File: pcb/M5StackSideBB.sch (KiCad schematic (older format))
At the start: 4 parts, among them J1 Conn_01x15, J2 Conn_01x15, J3 Conn_02x15_Odd_Even, J4 Conn_02x15_Odd_Even

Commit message: Put components and holes as pcb
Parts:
- removed J1, J2: Conn_01x15, Connector_PinSocket_2.54mm:PinSocket_1x15_P2.54mm_Vertical, symbol Connector_Generic:Conn_01x15
- added J1: Conn_01x17, Connector_PinSocket_2.54mm:PinSocket_1x17_P2.54mm_Vertical, symbol Connector_Generic:Conn_01x17
- added J2: Conn_01x09, Connector_PinSocket_2.54mm:PinSocket_1x09_P2.54mm_Vertical, symbol Connector_Generic:Conn_01x09
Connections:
- net labels added: +3.3V
- net labels removed: 3V3

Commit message: Update schema and put silk texts
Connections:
- wire segments 42 -> 43
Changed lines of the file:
@@
 L power:+5V #PWR0114
 U 1 1 5B27E3D3
-P 5450 3350
-F 0 "#PWR0114" H 5450 3200 50  0001 C CNN
-F 1 "+5V" H 5465 3523 50  0000 C CNN
-F 2 "" H 5450 3350 50  0001 C CNN
-F 3 "" H 5450 3350 50  0001 C CNN
-	1    5450 3350
+P 5450 3450
+F 0 "#PWR0114" H 5450 3300 50  0001 C CNN
+F 1 "+5V" H 5465 3623 50  0000 C CNN
+F 2 "" H 5450 3450 50  0001 C CNN
+F 3 "" H 5450 3450 50  0001 C CNN
+	1    5450 3450
 	1    0    0    -1
 $EndComp
@@
 L power:+3.3V #PWR0115
 U 1 1 5B27E3D9
-P 5600 3250
-F 0 "#PWR0115" H 5600 3100 50  0001 C CNN
-F 1 "+3.3V" H 5615 3423 50  0000 C CNN
-F 2 "" H 5600 3250 50  0001 C CNN
-F 3 "" H 5600 3250 50  0001 C CNN
-	1    5600 3250
+P 5600 3350
+F 0 "#PWR0115" H 5600 3200 50  0001 C CNN
+F 1 "+3.3V" H 5615 3523 50  0000 C CNN
+F 2 "" H 5600 3350 50  0001 C CNN
+F 3 "" H 5600 3350 50  0001 C CNN
+	1    5600 3350
 	1    0    0    -1
 $EndComp
@@
 L power:GND #PWR0116
 U 1 1 5B27E3DF
-P 5750 3450
-F 0 "#PWR0116" H 5750 3200 50  0001 C CNN
-F 1 "GND" H 5755 3277 50  0000 C CNN
-F 2 "" H 5750 3450 50  0001 C CNN
-F 3 "" H 5750 3450 50  0001 C CNN
-	1    5750 3450
+P 5850 3650
+F 0 "#PWR0116" H 5850 3400 50  0001 C CNN
+F 1 "GND" H 5855 3477 50  0000 C CNN
+F 2 "" H 5850 3650 50  0001 C CNN
+F 3 "" H 5850 3650 50  0001 C CNN
+	1    5850 3650
 	1    0    0    -1
 $EndComp
 Wire Wire Line
-	6000 3250 5600 3250
+	6000 3350 5600 3350
 Wire Wire Line
-	6000 3350 5450 3350
-Wire Wire Line
-	6000 3450 5750 3450
+	6000 3450 5450 3450
 $Comp
 L Connector_Generic:Conn_01x09 J2
@@
 Wire Wire Line
 	3850 2000 4150 2000
+Wire Wire Line
+	6000 3250 5850 3250
+Wire Wire Line
+	5850 3250 5850 3650
 $EndSCHEMATC

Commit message: Change pinsocket on schema
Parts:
- removed J1: Conn_01x17, Connector_PinSocket_2.54mm:PinSocket_1x17_P2.54mm_Vertical, symbol Connector_Generic:Conn_01x17
- removed J2: Conn_01x09, Connector_PinSocket_2.54mm:PinSocket_1x09_P2.54mm_Vertical, symbol Connector_Generic:Conn_01x09
- added J1, J2: Conn_01x11, Connector_PinSocket_2.54mm:PinSocket_1x11_P2.54mm_Vertical, symbol Connector_Generic:Conn_01x11
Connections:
- wire segments 43 -> 36
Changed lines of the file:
@@
 Wire Wire Line
 	7750 2150 7750 2250
-$Comp
-L power:GND #PWR0102
-U 1 1 5B24A9FC
-P 4550 2250
-F 0 "#PWR0102" H 4550 2000 50  0001 C CNN
-F 1 "GND" H 4555 2077 50  0000 C CNN
-F 2 "" H 4550 2250 50  0001 C CNN
-F 3 "" H 4550 2250 50  0001 C CNN
-	1    4550 2250
-	1    0    0    -1
-$EndComp
-Text GLabel 4150 2500 0    39   Input ~ 0
+Text GLabel 4950 2350 0    39   Input ~ 0
 G2
-Text GLabel 6000 3150 0    39   Input ~ 0
+Text GLabel 6000 2950 0    39   Input ~ 0
 G21
-Text GLabel 4150 2300 0    39   Input ~ 0
+Text GLabel 6000 2550 0    39   Input ~ 0
 G16
-Text GLabel 4150 2100 0    39   Input ~ 0
+Text GLabel 6000 2350 0    39   Input ~ 0
 G3
 Text GLabel 6000 2750 0    39   Input ~ 0
@@
 Text GLabel 6000 2850 0    39   Input ~ 0
 G19
-Text GLabel 6000 2950 0    39   Input ~ 0
+Text GLabel 6000 3150 0    39   Input ~ 0
 G23
 Text GLabel 7600 3450 0    39   Input ~ 0
@@
 Wire Wire Line
 	7800 3350 7900 3350
-Connection ~ 7800 3350
 Wire Wire Line
 	7800 3350 7800 3450
@@
 Text GLabel 7900 3050 0    39   Input ~ 0
 G12
-Text GLabel 7900 2950 0    39   Input ~ 0
-G2
-Text GLabel 7900 2850 0    39   Input ~ 0
-G21
-Text GLabel 7900 2750 0    39   Input ~ 0
-G16
-Text GLabel 7900 2650 0    39   Input ~ 0
-G3
-Text GLabel 7900 2550 0    39   Input ~ 0
-G18
-Text GLabel 7900 2450 0    39   Input ~ 0
-G19
-Text GLabel 7900 2350 0    39   Input ~ 0
-G23
-Text GLabel 4150 2900 0    39   Input ~ 0
+Text GLabel 4950 2750 0    39   Input ~ 0
 G35
-Text GLabel 4150 3000 0    39   Input ~ 0
+Text GLabel 4950 2850 0    39   Input ~ 0
 G36
-Text GLabel 4150 3100 0    39   Input ~ 0
+Text GLabel 4950 2950 0    39   Input ~ 0
 RST
-Text GLabel 4150 2700 0    39   Input ~ 0
+Text GLabel 4950 2550 0    39   Input ~ 0
 G25
-Text GLabel 4150 2800 0    39   Input ~ 0
+Text GLabel 4950 2650 0    39   Input ~ 0
 G26
-Text GLabel 4150 2200 0    39   Input ~ 0
+Text GLabel 6000 2450 0    39   Input ~ 0
 G1
-Text GLabel 4150 2400 0    39   Input ~ 0
+Text GLabel 6000 2650 0    39   Input ~ 0
 G17
 Text GLabel 6000 3050 0    39   Input ~ 0
 G22
-Text GLabel 4150 2600 0    39   Input ~ 0
+Text GLabel 4950 2450 0    39   Input ~ 0
 G5
 $Comp
 L power:+5V #PWR0103
 U 1 1 5B24B644
-P 3600 3400
-F 0 "#PWR0103" H 3600 3250 50  0001 C CNN
-F 1 "+5V" H 3615 3573 50  0000 C CNN
-F 2 "" H 3600 3400 50  0001 C CNN
-F 3 "" H 3600 3400 50  0001 C CNN
-	1    3600 3400
+P 4400 3250
+F 0 "#PWR0103" H 4400 3100 50  0001 C CNN
+F 1 "+5V" H 4415 3423 50  0000 C CNN
+F 2 "" H 4400 3250 50  0001 C CNN
+F 3 "" H 4400 3250 50  0001 C CNN
+	1    4400 3250
 	1    0    0    -1
 $EndComp
@@
 L power:+BATT #PWR0104
 U 1 1 5B24B943
-P 3900 3200
-F 0 "#PWR0104" H 3900 3050 50  0001 C CNN
-F 1 "+BATT" H 3915 3373 50  0000 C CNN
-F 2 "" H 3900 3200 50  0001 C CNN
-F 3 "" H 3900 3200 50  0001 C CNN
-	1    3900 3200
+P 4700 3050
+F 0 "#PWR0104" H 4700 2900 50  0001 C CNN
+F 1 "+BATT" H 4715 3223 50  0000 C CNN
+F 2 "" H 4700 3050 50  0001 C CNN
+F 3 "" H 4700 3050 50  0001 C CNN
+	1    4700 3050
 	1    0    0    -1
 $EndComp
@@
 	8550 4500 8550 4600
 $Comp
-L Connector_Generic:Conn_01x17 J1
-U 1 1 5B27A34A
-P 4350 2700
-F 0 "J1" H 4350 3750 50  0000 L CNN
-F 1 "Conn_01x17" H 4200 3650 50  0000 L CNN
-F 2 "Connector_PinSocket_2.54mm:PinSocket_1x17_P2.54mm_Vertical" H 4350 2700 50  0001 C CNN
-F 3 "~" H 4350 2700 50  0001 C CNN
-	1    4350 2700
-	1    0    0    -1
-$EndComp
-$Comp
 L power:+3.3V #PWR0110
 U 1 1 5B27AF84
-P 3750 3300
-F 0 "#PWR0110" H 3750 3150 50  0001 C CNN
-F 1 "+3.3V" H 3765 3473 50  0000 C CNN
-F 2 "" H 3750 3300 50  0001 C CNN
-F 3 "" H 3750 3300 50  0001 C CNN
-	1    3750 3300
+P 4550 3150
+F 0 "#PWR0110" H 4550 3000 50  0001 C CNN
+F 1 "+3.3V" H 4565 3323 50  0000 C CNN
+F 2 "" H 4550 3150 50  0001 C CNN
+F 3 "" H 4550 3150 50  0001 C CNN
+	1    4550 3150
 	1    0    0    -1
 $EndComp
@@
 L power:GND #PWR0111
 U 1 1 5B27AFCA
-P 3900 3500
-F 0 "#PWR0111" H 3900 3250 50  0001 C CNN
-F 1 "GND" H 3905 3327 50  0000 C CNN
-F 2 "" H 3900 3500 50  0001 C CNN
-F 3 "" H 3900 3500 50  0001 C CNN
-	1    3900 3500
+P 4700 3350
+F 0 "#PWR0111" H 4700 3100 50  0001 C CNN
+F 1 "GND" H 4705 3177 50  0000 C CNN
+F 2 "" H 4700 3350 50  0001 C CNN
+F 3 "" H 4700 3350 50  0001 C CNN
+	1    4700 3350
 	1    0    0    -1
 $EndComp
@@
 	7900 4900 7500 4900
 Wire Wire Line
-	4150 3200 3900 3200
-Wire Wire Line
-	4150 3300 3750 3300
-Wire Wire Line
-	4150 3400 3600 3400
-Wire Wire Line
-	4150 3500 3900 3500
-$Comp
-L power:+5V #PWR0114
-U 1 1 5B27E3D3
-P 5450 3450
-F 0 "#PWR0114" H 5450 3300 50  0001 C CNN
-F 1 "+5V" H 5465 3623 50  0000 C CNN
-F 2 "" H 5450 3450 50  0001 C CNN
-F 3 "" H 5450 3450 50  0001 C CNN
-	1    5450 3450
-	1    0    0    -1
-$EndComp
+	4950 3050 4700 3050
+Wire Wire Line
+	4950 3150 4550 3150
+Wire Wire Line
+	4950 3250 4400 3250
+Wire Wire Line
+	4950 3350 4700 3350
 $Comp
 L power:+3.3V #PWR0115
 U 1 1 5B27E3D9
-P 5600 3350
-F 0 "#PWR0115" H 5600 3200 50  0001 C CNN
-F 1 "+3.3V" H 5615 3523 50  0000 C CNN
-F 2 "" H 5600 3350 50  0001 C CNN
-F 3 "" H 5600 3350 50  0001 C CNN
-	1    5600 3350
+P 5600 3250
+F 0 "#PWR0115" H 5600 3100 50  0001 C CNN
+F 1 "+3.3V" H 5615 3423 50  0000 C CNN
+F 2 "" H 5600 3250 50  0001 C CNN
+F 3 "" H 5600 3250 50  0001 C CNN
+	1    5600 3250
 	1    0    0    -1
 $EndComp
@@
 L power:GND #PWR0116
 U 1 1 5B27E3DF
-P 5850 3650
-F 0 "#PWR0116" H 5850 3400 50  0001 C CNN
-F 1 "GND" H 5855 3477 50  0000 C CNN
-F 2 "" H 5850 3650 50  0001 C CNN
-F 3 "" H 5850 3650 50  0001 C CNN
-	1    5850 3650
-	1    0    0    -1
-$EndComp
-Wire Wire Line
-	6000 3350 5600 3350
-Wire Wire Line
-	6000 3450 5450 3450
-$Comp
-L Connector_Generic:Conn_01x09 J2
-U 1 1 5B27F564
-P 6200 3050
-F 0 "J2" H 6150 3750 50  0000 L CNN
-F 1 "Conn_01x09" H 6100 3650 50  0000 L CNN
-F 2 "Connector_PinSocket_2.54mm:PinSocket_1x09_P2.54mm_Vertical" H 6200 3050 50  0001 C CNN
-F 3 "~" H 6200 3050 50  0001 C CNN
-	1    6200 3050
-	1    0    0    -1
-$EndComp
-$Comp
-L power:GND #PWR0117
-U 1 1 5B27F598
-P 5750 2650
-F 0 "#PWR0117" H 5750 2400 50  0001 C CNN
-F 1 "GND" H 5755 2477 50  0000 C CNN
-F 2 "" H 5750 2650 50  0001 C CNN
-F 3 "" H 5750 2650 50  0001 C CNN
-	1    5750 2650
-	1    0    0    -1
-$EndComp
-Wire Wire Line
-	6000 2650 5750 2650
-$Comp
-L power:GND #PWR0118
-U 1 1 5B27FF4C
-P 3750 1900
-F 0 "#PWR0118" H 3750 1650 50  0001 C CNN
-F 1 "GND" H 3755 1727 50  0000 C CNN
-F 2 "" H 3750 1900 50  0001 C CNN
-F 3 "" H 3750 1900 50  0001 C CNN
-	1    3750 1900
-	1    0    0    -1
-$EndComp
-Wire Wire Line
-	4150 1900 3750 1900
-$Comp
-L power:+3.3V #PWR0119
-U 1 1 5B280891
-P 3550 2200
-F 0 "#PWR0119" H 3550 2050 50  0001 C CNN
-F 1 "+3.3V" H 3565 2373 50  0000 C CNN
-F 2 "" H 3550 2200 50  0001 C CNN
-F 3 "" H 3550 2200 50  0001 C CNN
-	1    3550 2200
-	1    0    0    -1
-$EndComp
-Wire Wire Line
-	3550 2200 3850 2200
-Wire Wire Line
-	3850 2200 3850 2000
-Wire Wire Line
-	3850 2000 4150 2000
-Wire Wire Line
-	6000 3250 5850 3250
-Wire Wire Line
-	5850 3250 5850 3650
+P 5850 3350
+F 0 "#PWR0116" H 5850 3100 50  0001 C CNN
+F 1 "GND" H 5855 3177 50  0000 C CNN
+F 2 "" H 5850 3350 50  0001 C CNN
+F 3 "" H 5850 3350 50  0001 C CNN
+	1    5850 3350
+	1    0    0    -1
+$EndComp
+Wire Wire Line
+	6000 3250 5600 3250
+Text GLabel 7900 2950 0    39   Input ~ 0
+G2
+Text GLabel 7900 2850 0    39   Input ~ 0
+G21
+Text GLabel 7900 2750 0    39   Input ~ 0
+G16
+Text GLabel 7900 2650 0    39   Input ~ 0
+G3
+Text GLabel 7900 2550 0    39   Input ~ 0
+G18
+Text GLabel 7900 2450 0    39   Input ~ 0
+G19
+Text GLabel 7900 2350 0    39   Input ~ 0
+G23
+Connection ~ 7800 3350
+$Comp
+L Connector_Generic:Conn_01x11 J1
+U 1 1 5B50BA11
+P 5150 2850
+F 0 "J1" H 5150 3600 50  0000 L CNN
+F 1 "Conn_01x11" H 5000 3500 50  0000 L CNN
+F 2 "Connector_PinSocket_2.54mm:PinSocket_1x11_P2.54mm_Vertical" H 5150 2850 50  0001 C CNN
+F 3 "~" H 5150 2850 50  0001 C CNN
+	1    5150 2850
+	1    0    0    -1
+$EndComp
+$Comp
+L Connector_Generic:Conn_01x11 J2
+U 1 1 5B50C22A
+P 6200 2850
+F 0 "J2" H 6200 3600 50  0000 L CNN
+F 1 "Conn_01x11" H 6050 3500 50  0000 L CNN
+F 2 "Connector_PinSocket_2.54mm:PinSocket_1x11_P2.54mm_Vertical" H 6200 2850 50  0001 C CNN
+F 3 "~" H 6200 2850 50  0001 C CNN
+	1    6200 2850
+	1    0    0    -1
+$EndComp
+Wire Wire Line
+	6000 3350 5850 3350
 $EndSCHEMATC

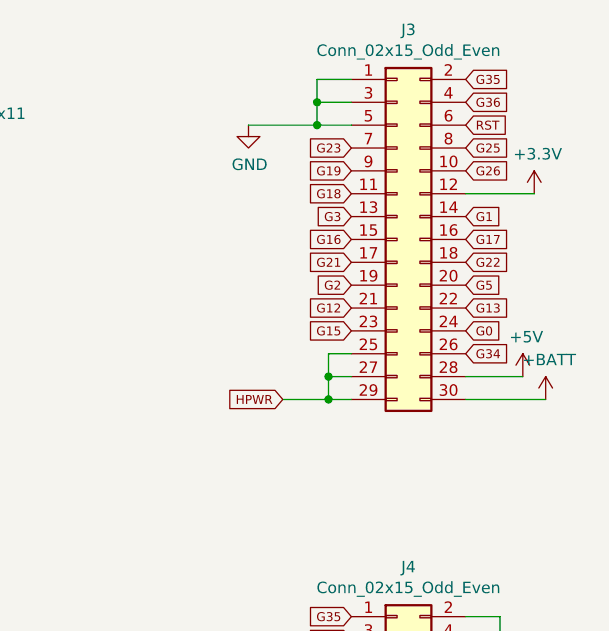
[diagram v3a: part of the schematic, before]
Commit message: Correct pin assign for bottom socket
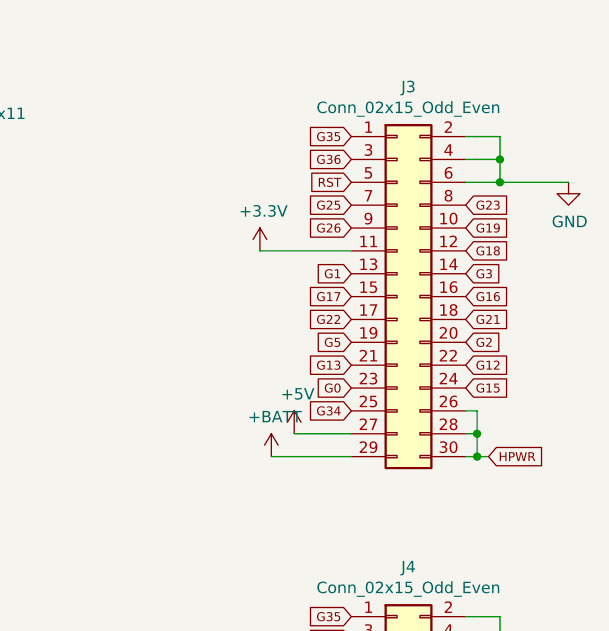
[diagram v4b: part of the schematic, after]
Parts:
- J3: footprint Connector_PinSocket_2.54mm:PinSocket_2x15_P2.54mm_Vertical_SMD -> footprints:PinHeader_2x15_P2.54mm_Vertical_SMD_for_plate
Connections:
- net +3V3: now also J3.11 (Pin_11); no longer J3.12 (Pin_12)
- net +5V: now also J3.27 (Pin_27); no longer J3.28 (Pin_28)
- net +BATT: now also J3.29 (Pin_29); no longer J3.30 (Pin_30)
- net G0: now also J3.23 (Pin_23); no longer J3.24 (Pin_24)
- net G1: now also J3.13 (Pin_13); no longer J3.14 (Pin_14)
- net G12: now also J3.22 (Pin_22); no longer J3.21 (Pin_21)
- net G13: now also J3.21 (Pin_21); no longer J3.22 (Pin_22)
- net G15: now also J3.24 (Pin_24); no longer J3.23 (Pin_23)
- net G16: now also J3.16 (Pin_16); no longer J3.15 (Pin_15)
- net G17: now also J3.15 (Pin_15); no longer J3.16 (Pin_16)
- net G18: now also J3.12 (Pin_12); no longer J3.11 (Pin_11)
- net G19: now also J3.10 (Pin_10); no longer J3.9 (Pin_9)
- net G2: now also J3.20 (Pin_20); no longer J3.19 (Pin_19)
- net G21: now also J3.18 (Pin_18); no longer J3.17 (Pin_17)
- net G22: now also J3.17 (Pin_17); no longer J3.18 (Pin_18)
- net G23: now also J3.8 (Pin_8); no longer J3.7 (Pin_7)
- net G25: now also J3.7 (Pin_7); no longer J3.8 (Pin_8)
- net G26: now also J3.9 (Pin_9); no longer J3.10 (Pin_10)
- net G3: now also J3.14 (Pin_14); no longer J3.13 (Pin_13)
- net G34: now also J3.25 (Pin_25); no longer J3.26 (Pin_26)
- net G35: now also J3.1 (Pin_1); no longer J3.2 (Pin_2)
- net G36: now also J3.3 (Pin_3); no longer J3.4 (Pin_4)
- net G5: now also J3.19 (Pin_19); no longer J3.20 (Pin_20)
- net GND: now also J3.2 (Pin_2), J3.4 (Pin_4), J3.6 (Pin_6); no longer J3.1 (Pin_1), J3.3 (Pin_3), J3.5 (Pin_5)
- net HPWR: now also J3.26 (Pin_26), J3.28 (Pin_28), J3.30 (Pin_30); no longer J3.25 (Pin_25), J3.27 (Pin_27), J3.29 (Pin_29)
- net RST: now also J3.5 (Pin_5); no longer J3.6 (Pin_6)
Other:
- moved on the sheet: J3
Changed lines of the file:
@@
 L Connector_Generic:Conn_02x15_Odd_Even J3
 U 1 1 5B24A05D
-P 8100 2750
-F 0 "J3" H 8150 3667 50  0000 C CNN
-F 1 "Conn_02x15_Odd_Even" H 8150 3576 50  0000 C CNN
-F 2 "Connector_PinSocket_2.54mm:PinSocket_2x15_P2.54mm_Vertical_SMD" H 8100 2750 50  0001 C CNN
-F 3 "~" H 8100 2750 50  0001 C CNN
-	1    8100 2750
-	1    0    0    -1
-$EndComp
-$Comp
-L power:GND #PWR0101
-U 1 1 5B24A244
-P 7450 2250
-F 0 "#PWR0101" H 7450 2000 50  0001 C CNN
-F 1 "GND" H 7455 2077 50  0000 C CNN
-F 2 "" H 7450 2250 50  0001 C CNN
-F 3 "" H 7450 2250 50  0001 C CNN
-	1    7450 2250
-	1    0    0    -1
-$EndComp
-Wire Wire Line
-	7450 2250 7750 2250
-Wire Wire Line
-	7900 2050 7750 2050
-Wire Wire Line
-	7750 2050 7750 2150
-Connection ~ 7750 2250
-Wire Wire Line
-	7750 2250 7900 2250
-Wire Wire Line
-	7900 2150 7750 2150
-Connection ~ 7750 2150
-Wire Wire Line
-	7750 2150 7750 2250
+P 8100 3000
+F 0 "J3" H 8150 3917 50  0000 C CNN
+F 1 "Conn_02x15_Odd_Even" H 8150 3826 50  0000 C CNN
+F 2 "footprints:PinHeader_2x15_P2.54mm_Vertical_SMD_for_plate" H 8100 3000 50  0001 C CNN
+F 3 "~" H 8100 3000 50  0001 C CNN
+	1    8100 3000
+	1    0    0    -1
+$EndComp
 Text GLabel 4950 2350 0    39   Input ~ 0
 G2
@@
 Text GLabel 6000 3150 0    39   Input ~ 0
 G23
-Text GLabel 7600 3450 0    39   Input ~ 0
-HPWR
-Wire Wire Line
-	7600 3450 7800 3450
-Wire Wire Line
-	7900 3250 7800 3250
-Wire Wire Line
-	7800 3250 7800 3350
-Connection ~ 7800 3450
-Wire Wire Line
-	7800 3450 7900 3450
-Wire Wire Line
-	7800 3350 7900 3350
-Wire Wire Line
-	7800 3350 7800 3450
-Text GLabel 7900 3150 0    39   Input ~ 0
-G15
-Text GLabel 7900 3050 0    39   Input ~ 0
-G12
 Text GLabel 4950 2750 0    39   Input ~ 0
 G35
@@
 Wire Wire Line
 	7550 5800 7900 5800
-Text GLabel 8400 2050 2    39   Input ~ 0
-G35
-Text GLabel 8400 2150 2    39   Input ~ 0
-G36
-Text GLabel 8400 2250 2    39   Input ~ 0
-RST
-Text GLabel 8400 2350 2    39   Input ~ 0
-G25
-Text GLabel 8400 2450 2    39   Input ~ 0
-G26
-Text GLabel 8400 2650 2    39   Input ~ 0
-G1
-Text GLabel 8400 2750 2    39   Input ~ 0
-G17
-Text GLabel 8400 2850 2    39   Input ~ 0
-G22
-Text GLabel 8400 2950 2    39   Input ~ 0
-G5
-Text GLabel 8400 3050 2    39   Input ~ 0
-G13
-Text GLabel 8400 3150 2    39   Input ~ 0
-G0
-Text GLabel 8400 3250 2    39   Input ~ 0
-G34
-$Comp
-L power:+5V #PWR0107
-U 1 1 5B24CA2B
-P 8650 3350
-F 0 "#PWR0107" H 8650 3200 50  0001 C CNN
-F 1 "+5V" H 8665 3523 50  0000 C CNN
-F 2 "" H 8650 3350 50  0001 C CNN
-F 3 "" H 8650 3350 50  0001 C CNN
-	1    8650 3350
-	1    0    0    -1
-$EndComp
-$Comp
-L power:+BATT #PWR0108
-U 1 1 5B24CA3E
-P 8750 3450
-F 0 "#PWR0108" H 8750 3300 50  0001 C CNN
-F 1 "+BATT" H 8765 3623 50  0000 C CNN
-F 2 "" H 8750 3450 50  0001 C CNN
-F 3 "" H 8750 3450 50  0001 C CNN
-	1    8750 3450
-	1    0    0    -1
-$EndComp
-Wire Wire Line
-	8400 3350 8650 3350
-Wire Wire Line
-	8400 3450 8750 3450
 Text GLabel 8400 4700 2    39   Input ~ 0
 G23
@@
 $EndComp
 $Comp
-L power:+3.3V #PWR0112
-U 1 1 5B27B055
-P 8700 2550
-F 0 "#PWR0112" H 8700 2400 50  0001 C CNN
-F 1 "+3.3V" H 8715 2723 50  0000 C CNN
-F 2 "" H 8700 2550 50  0001 C CNN
-F 3 "" H 8700 2550 50  0001 C CNN
-	1    8700 2550
-	1    0    0    -1
-$EndComp
-Wire Wire Line
-	8400 2550 8700 2550
-$Comp
 L power:+3.3V #PWR0113
 U 1 1 5B27B63E
@@
 Wire Wire Line
 	6000 3250 5600 3250
-Text GLabel 7900 2950 0    39   Input ~ 0
-G2
-Text GLabel 7900 2850 0    39   Input ~ 0
-G21
-Text GLabel 7900 2750 0    39   Input ~ 0
-G16
-Text GLabel 7900 2650 0    39   Input ~ 0
-G3
-Text GLabel 7900 2550 0    39   Input ~ 0
-G18
-Text GLabel 7900 2450 0    39   Input ~ 0
-G19
-Text GLabel 7900 2350 0    39   Input ~ 0
-G23
-Connection ~ 7800 3350
 $Comp
 L Connector_Generic:Conn_01x11 J1
@@
 Wire Wire Line
 	6000 3350 5850 3350
+Text GLabel 7900 2300 0    39   Input ~ 0
+G35
+Text GLabel 7900 2400 0    39   Input ~ 0
+G36
+Text GLabel 7900 2500 0    39   Input ~ 0
+RST
+Text GLabel 7900 2600 0    39   Input ~ 0
+G25
+Text GLabel 7900 2700 0    39   Input ~ 0
+G26
+Text GLabel 7900 2900 0    39   Input ~ 0
+G1
+Text GLabel 7900 3000 0    39   Input ~ 0
+G17
+Text GLabel 7900 3100 0    39   Input ~ 0
+G22
+Text GLabel 7900 3200 0    39   Input ~ 0
+G5
+Text GLabel 7900 3300 0    39   Input ~ 0
+G13
+Text GLabel 7900 3400 0    39   Input ~ 0
+G0
+Text GLabel 7900 3500 0    39   Input ~ 0
+G34
+$Comp
+L power:+5V #PWR?
+U 1 1 5B50EF03
+P 7650 3600
+F 0 "#PWR?" H 7650 3450 50  0001 C CNN
+F 1 "+5V" H 7665 3773 50  0000 C CNN
+F 2 "" H 7650 3600 50  0001 C CNN
+F 3 "" H 7650 3600 50  0001 C CNN
+	1    7650 3600
+	1    0    0    -1
+$EndComp
+Wire Wire Line
+	7900 3600 7650 3600
+$Comp
+L power:+BATT #PWR?
+U 1 1 5B50EF0A
+P 7550 3700
+F 0 "#PWR?" H 7550 3550 50  0001 C CNN
+F 1 "+BATT" H 7565 3873 50  0000 C CNN
+F 2 "" H 7550 3700 50  0001 C CNN
+F 3 "" H 7550 3700 50  0001 C CNN
+	1    7550 3700
+	1    0    0    -1
+$EndComp
+Wire Wire Line
+	7550 3700 7900 3700
+Text GLabel 8400 2600 2    39   Input ~ 0
+G23
+Text GLabel 8400 2700 2    39   Input ~ 0
+G19
+Text GLabel 8400 2800 2    39   Input ~ 0
+G18
+Text GLabel 8400 2900 2    39   Input ~ 0
+G3
+Text GLabel 8400 3000 2    39   Input ~ 0
+G16
+Text GLabel 8400 3100 2    39   Input ~ 0
+G21
+Text GLabel 8400 3200 2    39   Input ~ 0
+G2
+Text GLabel 8400 3300 2    39   Input ~ 0
+G12
+Text GLabel 8400 3400 2    39   Input ~ 0
+G15
+Text GLabel 8500 3700 2    39   Input ~ 0
+HPWR
+Wire Wire Line
+	8400 3700 8450 3700
+Wire Wire Line
+	8450 3700 8450 3600
+Wire Wire Line
+	8450 3500 8400 3500
+Connection ~ 8450 3700
+Wire Wire Line
+	8450 3700 8500 3700
+Wire Wire Line
+	8400 3600 8450 3600
+Connection ~ 8450 3600
+Wire Wire Line
+	8450 3600 8450 3500
+$Comp
+L power:GND #PWR?
+U 1 1 5B50EF23
+P 8850 2500
+F 0 "#PWR?" H 8850 2250 50  0001 C CNN
+F 1 "GND" H 8855 2327 50  0000 C CNN
+F 2 "" H 8850 2500 50  0001 C CNN
+F 3 "" H 8850 2500 50  0001 C CNN
+	1    8850 2500
+	1    0    0    -1
+$EndComp
+Wire Wire Line
+	8400 2500 8550 2500
+Wire Wire Line
+	8400 2300 8550 2300
+Wire Wire Line
+	8550 2300 8550 2400
+Connection ~ 8550 2500
+Wire Wire Line
+	8550 2500 8850 2500
+Wire Wire Line
+	8400 2400 8550 2400
+Connection ~ 8550 2400
+Wire Wire Line
+	8550 2400 8550 2500
+$Comp
+L power:+3.3V #PWR?
+U 1 1 5B50EF31
+P 7500 2800
+F 0 "#PWR?" H 7500 2650 50  0001 C CNN
+F 1 "+3.3V" H 7515 2973 50  0000 C CNN
+F 2 "" H 7500 2800 50  0001 C CNN
+F 3 "" H 7500 2800 50  0001 C CNN
+	1    7500 2800
+	1    0    0    -1
+$EndComp
+Wire Wire Line
+	7900 2800 7500 2800
 $EndSCHEMATC

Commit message: Update component and its position on pcb
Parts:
- J3: footprint footprints:PinHeader_2x15_P2.54mm_Vertical_SMD_for_plate -> footprints:PinHeader_2x15_P2.54mm_Vertical_SMD_for_M5Stack_top
- J4: footprint Connector_PinHeader_2.54mm:PinHeader_2x15_P2.54mm_Vertical_SMD -> footprints:PinSocket_2x15_P2.54mm_Vertical_SMD_for_M5Stack_bottom
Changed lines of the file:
@@
 F 0 "J3" H 8150 3917 50  0000 C CNN
 F 1 "Conn_02x15_Odd_Even" H 8150 3826 50  0000 C CNN
-F 2 "footprints:PinHeader_2x15_P2.54mm_Vertical_SMD_for_plate" H 8100 3000 50  0001 C CNN
+F 2 "footprints:PinHeader_2x15_P2.54mm_Vertical_SMD_for_M5Stack_top" H 8100 3000 50  0001 C CNN
 F 3 "~" H 8100 3000 50  0001 C CNN
 	1    8100 3000
@@
 F 0 "J4" H 8150 6017 50  0000 C CNN
 F 1 "Conn_02x15_Odd_Even" H 8150 5926 50  0000 C CNN
-F 2 "Connector_PinHeader_2.54mm:PinHeader_2x15_P2.54mm_Vertical_SMD" H 8100 5100 50  0001 C CNN
+F 2 "footprints:PinSocket_2x15_P2.54mm_Vertical_SMD_for_M5Stack_bottom" H 8100 5100 50  0001 C CNN
 F 3 "~" H 8100 5100 50  0001 C CNN
 	1    8100 5100
